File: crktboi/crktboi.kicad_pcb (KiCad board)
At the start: 2 copper layers, 66 x 21.5 mm, 32 parts, among them Q1 BC847, Q2 BC847, Q3 2N7002, Q4 2N7002, Q5 AO3401A, U1 GSC1102YB-3V4000, U2 VBPW34S, U3 VBPW34S, U4 BQ25505RGRT

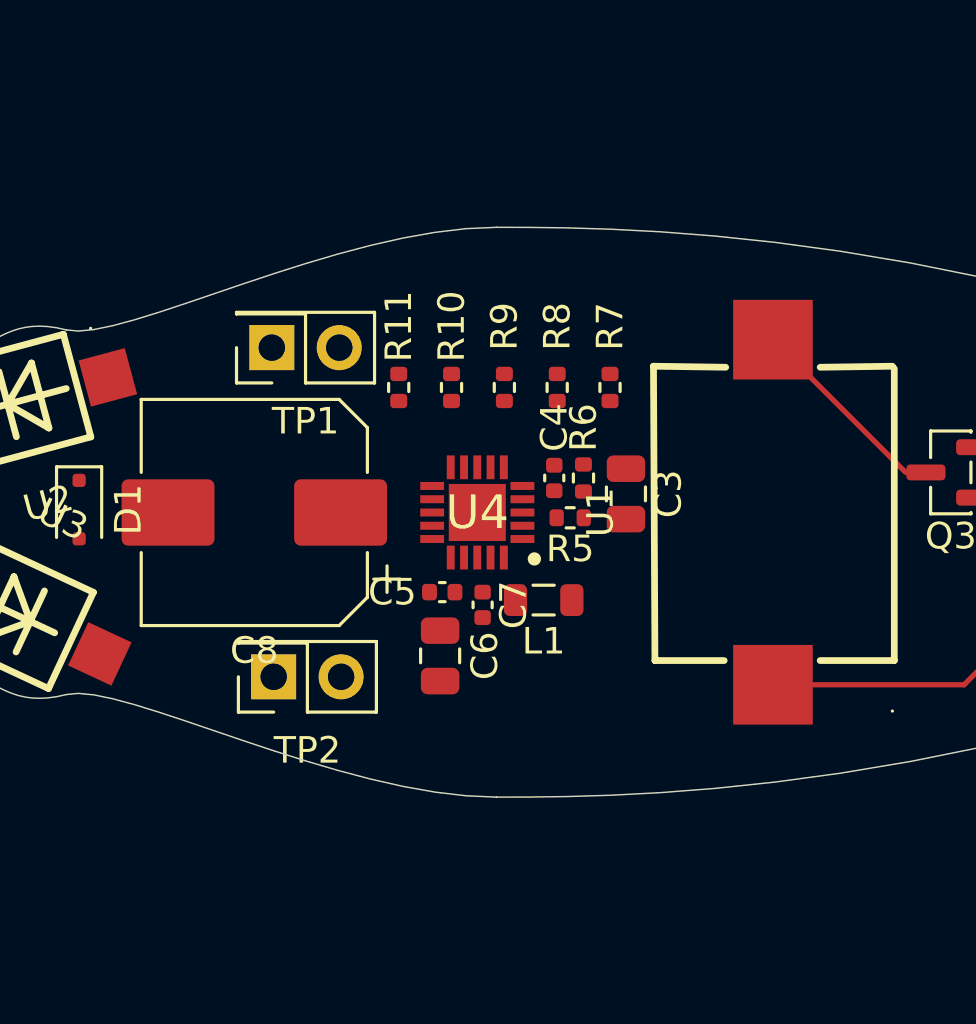
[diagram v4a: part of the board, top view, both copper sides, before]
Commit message: Added resistors as legs for the cicada and updated LCSC part numbers for new parts
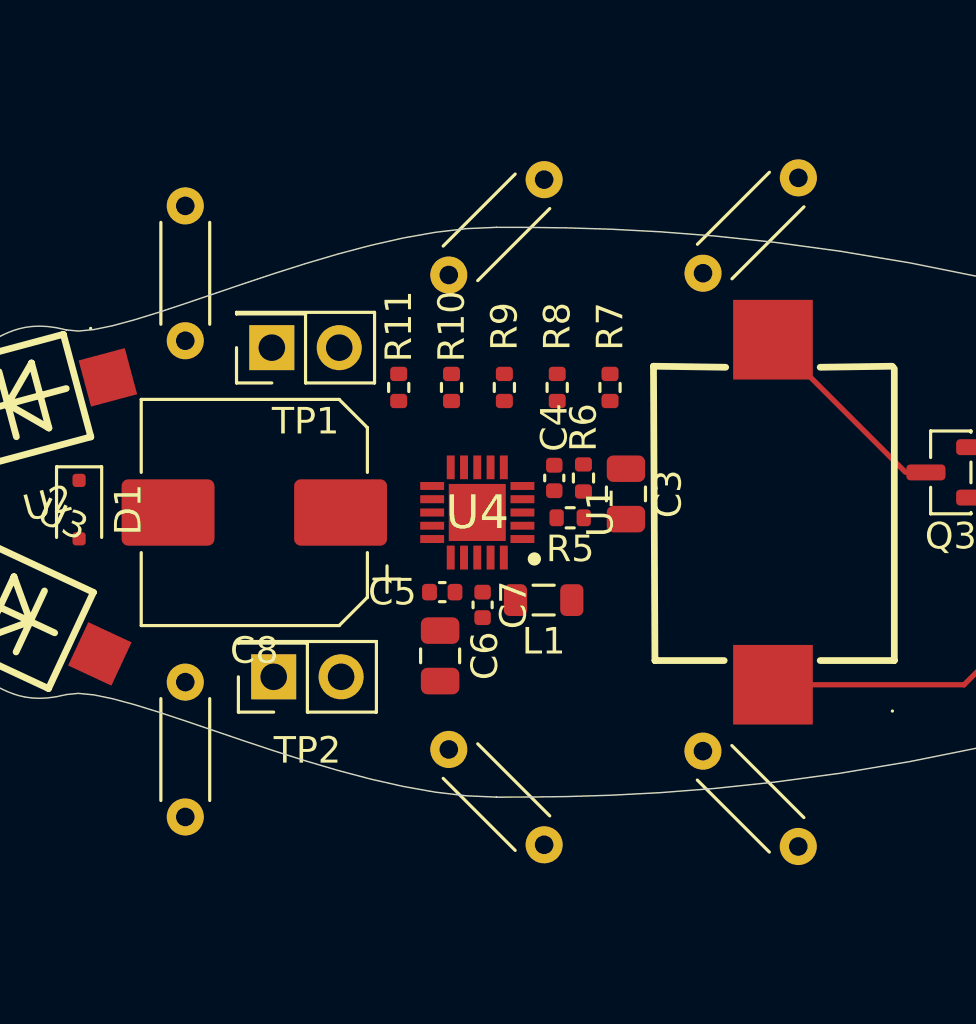
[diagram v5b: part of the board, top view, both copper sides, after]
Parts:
- added R12: R, Resistor_THT:R_Axial_DIN0204_L3.6mm_D1.6mm_P5.08mm_Horizontal, F.Cu at (138.2, 91.1)
- added R13: R, Resistor_THT:R_Axial_DIN0204_L3.6mm_D1.6mm_P5.08mm_Horizontal, F.Cu at (128.3, 93.5)
- added R14: R, Resistor_THT:R_Axial_DIN0204_L3.6mm_D1.6mm_P5.08mm_Horizontal, F.Cu at (147.8, 91.0)
- added R15: R, Resistor_THT:R_Axial_DIN0204_L3.6mm_D1.6mm_P5.08mm_Horizontal, F.Cu at (128.3, 111.5)
- added R16: R, Resistor_THT:R_Axial_DIN0204_L3.6mm_D1.6mm_P5.08mm_Horizontal, F.Cu at (147.8, 109.0)
- added R17: R, Resistor_THT:R_Axial_DIN0204_L3.6mm_D1.6mm_P5.08mm_Horizontal, F.Cu at (138.2, 108.9)

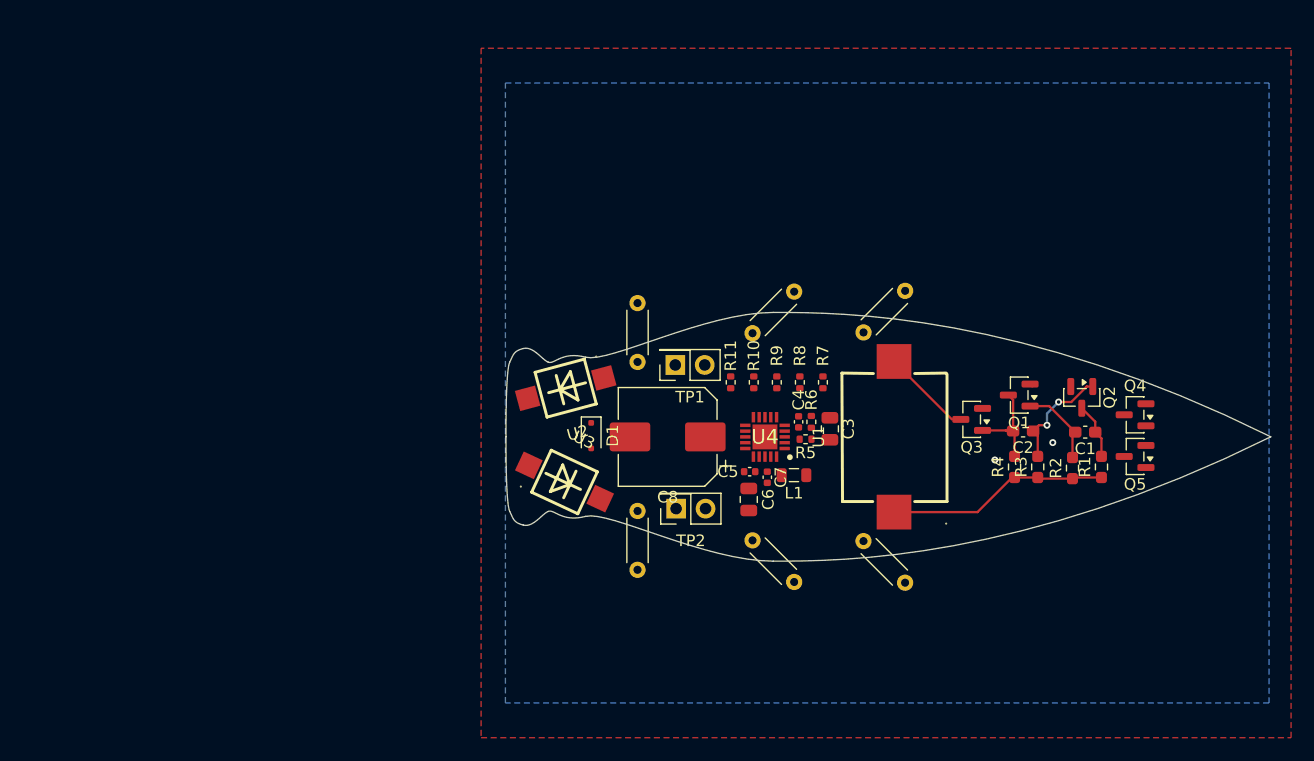
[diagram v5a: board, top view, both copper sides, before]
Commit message: Completed the board layout and ran through the DRC. Adjusted clearance limits to make it work
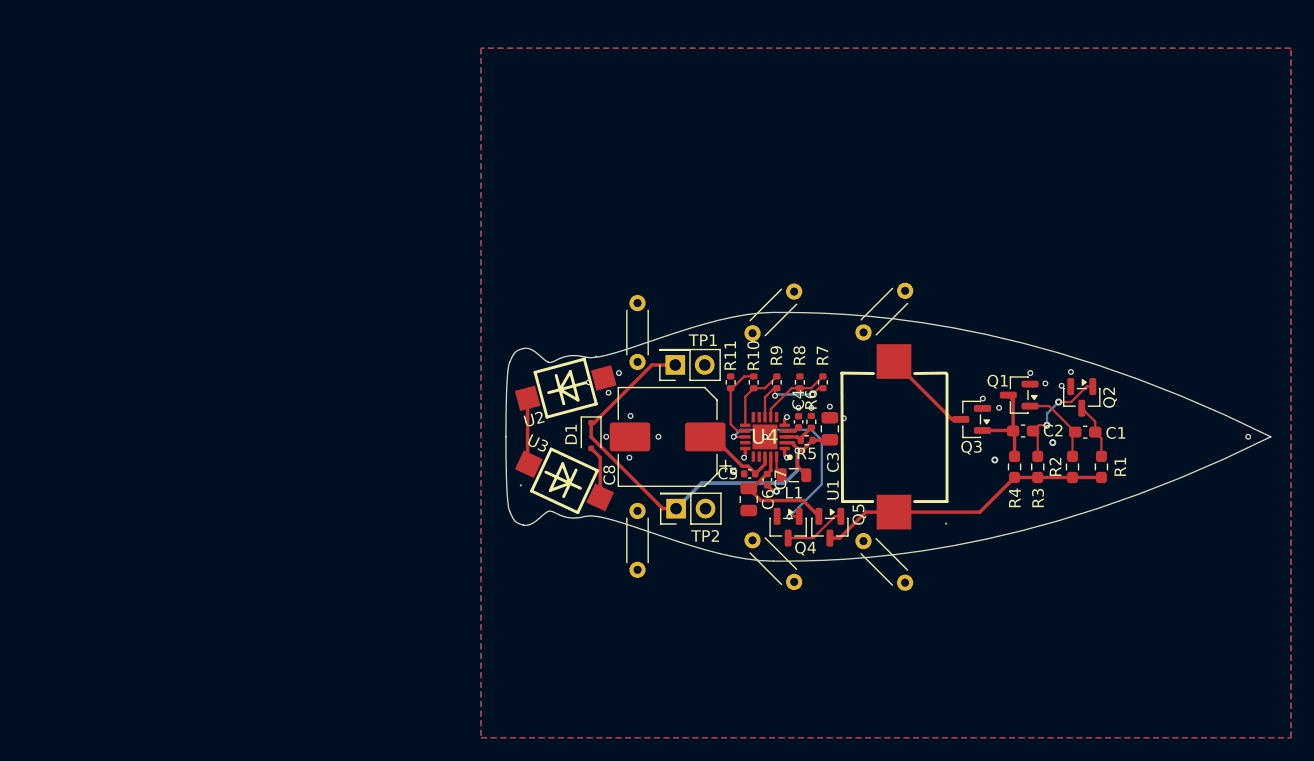
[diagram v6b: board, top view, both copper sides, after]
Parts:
- moved Q4 31.5 mm to (141.3, 107.8), turned to -90 degrees
- moved Q5 27.0 mm to (144.9, 107.8), turned to -90 degrees
- moved C7 0.21 mm to (139.5, 103.7)
- moved C5 0.19 mm to (138.0, 103.2)
- moved R5 0.13 mm to (142.9, 100.3)
- moved R2 0.10 mm to (165.8, 102.6)
- moved U3 0.10 mm to (122.0, 103.8)
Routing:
- net Net-(D1-K): track 0.00 -> 41.1 mm, vias 0 -> 1
- net /Power/VBAT_OK: track 0.00 -> 17.9 mm, vias 0 -> 2
- net /Power/Vstore: track 0.00 -> 9.94 mm
- net /Power/V_RDIV: track 0.00 -> 7.97 mm, vias 0 -> 2
- net /Power/OK_PROG: track 0.00 -> 6.87 mm
- net /Power/VCAP: track 0.00 -> 6.80 mm
- net +3V0: track 19.2 -> 25.6 mm
- net /Power/BAT_OV: track 0.00 -> 6.37 mm
- net /Power/OK_HYST: track 0.00 -> 5.91 mm
- net Net-(U2-C): track 0.00 -> 5.68 mm
- net Net-(Q4-D): track 0.00 -> 5.33 mm
- net Net-(D1-A): track 0.00 -> 4.56 mm
- net GND: track 0.30 -> 3.81 mm, vias 2 -> 26
- net Net-(U4-VOC_SAMP): track 0.00 -> 2.95 mm
- net Net-(U4-LBOOST): track 0.00 -> 1.78 mm
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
